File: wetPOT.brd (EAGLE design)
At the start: 38.1 x 12.7 mm, 2 parts

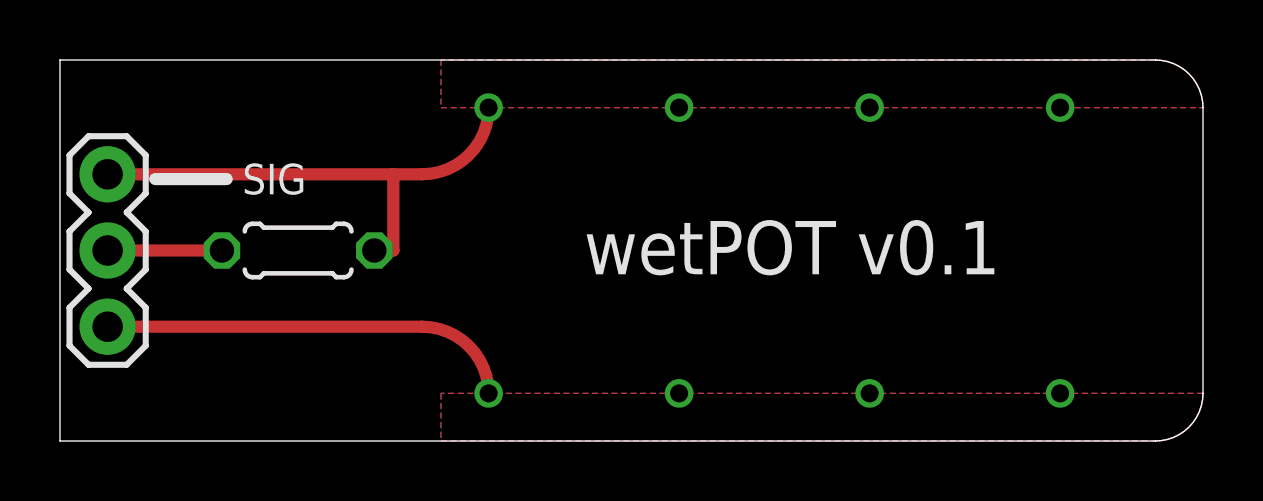
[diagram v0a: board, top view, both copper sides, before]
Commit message: Updated resistor to correct form factor.
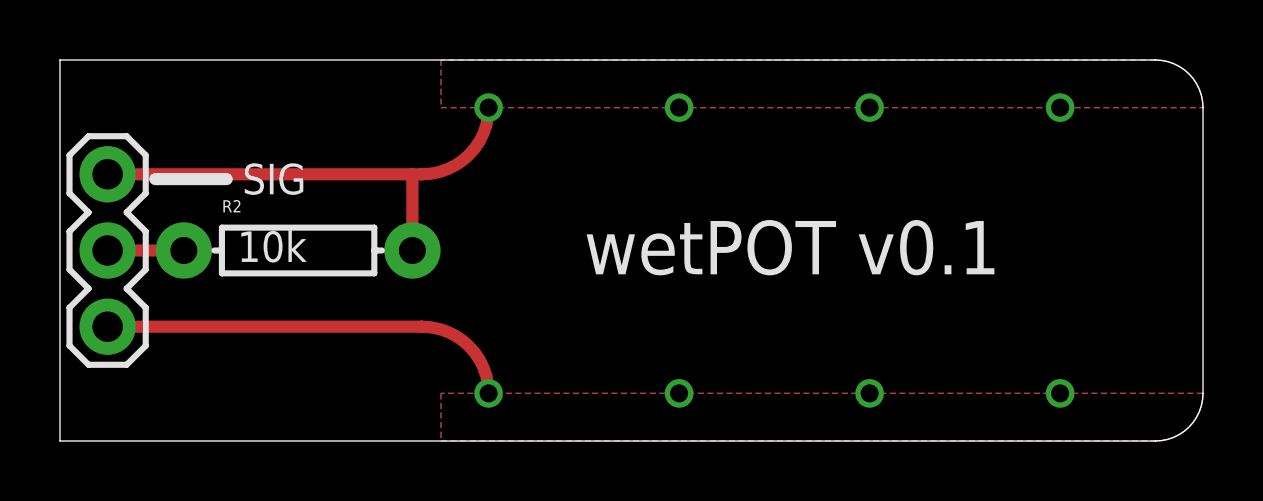
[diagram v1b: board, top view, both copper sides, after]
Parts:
- removed R1: 10k, resistor:0204/5
- added R2: 10k, SparkFun-Resistors:AXIAL-0.3
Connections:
- net PIN0: now also R2.P$2; no longer R1.2
- net PIN1: now also R2.P$1; no longer R1.1
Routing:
- net PIN1: track 3.81 -> 2.54 mm
- net PIN0: track 16.8 -> 16.2 mm
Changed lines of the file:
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@@
 <grid distance="0.03125" unitdist="inch" unit="inch" style="lines" multiple="1" display="yes" altdistance="0.025" altunitdist="inch" altunit="inch"/>
 <layers>
-<layer number="1" name="Top" color="4" fill="1" visible="no" active="yes"/>
-<layer number="16" name="Bottom" color="1" fill="1" visible="no" active="yes"/>
+<layer number="1" name="Top" color="4" fill="1" visible="yes" active="yes"/>
+<layer number="16" name="Bottom" color="1" fill="1" visible="yes" active="yes"/>
 <layer number="17" name="Pads" color="2" fill="1" visible="yes" active="yes"/>
 <layer number="18" name="Vias" color="2" fill="1" visible="yes" active="yes"/>
@@
 <layer number="223" name="223bmp" color="24" fill="1" visible="no" active="no"/>
 <layer number="224" name="224bmp" color="25" fill="1" visible="no" active="no"/>
+<layer number="225" name="225bmp" color="7" fill="1" visible="yes" active="yes"/>
+<layer number="226" name="226bmp" color="7" fill="1" visible="yes" active="yes"/>
+<layer number="227" name="227bmp" color="7" fill="1" visible="yes" active="yes"/>
+<layer number="228" name="228bmp" color="7" fill="1" visible="yes" active="yes"/>
+<layer number="229" name="229bmp" color="7" fill="1" visible="yes" active="yes"/>
+<layer number="230" name="230bmp" color="7" fill="1" visible="yes" active="yes"/>
+<layer number="231" name="231bmp" color="7" fill="1" visible="yes" active="yes"/>
 <layer number="248" name="Housing" color="7" fill="1" visible="yes" active="yes"/>
 <layer number="249" name="Edge" color="7" fill="1" visible="yes" active="yes"/>
@@
 </autorouter>
 <elements>
-<element name="R1" library="resistor" package="0204/5" value="10k" x="7.9375" y="6.35" smashed="yes"/>
 <element name="JP2" library="SparkFun-Connectors" package="1X03" value="" x="1.5875" y="3.81" smashed="yes" rot="R90">
 <attribute name="VALUE" x="4.7625" y="2.54" size="1.27" layer="27" rot="R90"/>
+</element>
+<element name="R2" library="SparkFun-Resistors" package="AXIAL-0.3" value="10k" x="7.9375" y="6.35">
+<attribute name="PROD_ID" value="RES-12183" x="7.9375" y="6.35" size="1.778" layer="27" display="off"/>
 </element>
 </elements>
 <signals>
 <signal name="PIN0">
-<contactref element="R1" pad="2"/>
 <contactref element="JP2" pad="3"/>
 <polygon width="0.4064" layer="1">
@@
 <via x="26.9875" y="11.1125" extent="1-16" drill="0.6" shape="octagon"/>
 <via x="33.3375" y="11.1125" extent="1-16" drill="0.6" shape="octagon"/>
-<wire x1="1.5875" y1="8.89" x2="11.1125" y2="8.89" width="0.4064" layer="1"/>
-<wire x1="11.1125" y1="8.89" x2="12.065" y2="8.89" width="0.4064" layer="1"/>
+<wire x1="1.5875" y1="8.89" x2="11.7475" y2="8.89" width="0.4064" layer="1"/>
 <wire x1="12.065" y1="8.89" x2="14.2875" y2="11.1125" width="0.4064" layer="1" curve="90"/>
-<wire x1="10.4775" y1="6.35" x2="11.1125" y2="6.35" width="0.4064" layer="1"/>
-<wire x1="11.1125" y1="6.35" x2="11.1125" y2="8.89" width="0.4064" layer="1"/>
+<contactref element="R2" pad="P$2"/>
+<wire x1="12.065" y1="8.89" x2="11.7475" y2="8.89" width="0.4064" layer="1"/>
+<wire x1="11.7475" y1="8.89" x2="11.7475" y2="6.35" width="0.4064" layer="1"/>
+<wire x1="26.9875" y1="11.1125" x2="33.3375" y2="11.1125" width="0" layer="19" extent="1-1"/>
+<wire x1="20.6375" y1="11.1125" x2="26.9875" y2="11.1125" width="0" layer="19" extent="1-1"/>
+<wire x1="14.2875" y1="11.1125" x2="20.6375" y2="11.1125" width="0" layer="19" extent="1-1"/>
 </signal>
 <signal name="PIN1">
-<contactref element="R1" pad="1"/>
 <contactref element="JP2" pad="2"/>
-<wire x1="1.5875" y1="6.35" x2="5.3975" y2="6.35" width="0.4064" layer="1"/>
+<contactref element="R2" pad="P$1"/>
+<wire x1="4.1275" y1="6.35" x2="1.5875" y2="6.35" width="0.4064" layer="1"/>
 </signal>
 <signal name="N$4">

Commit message: Turned resistor 90° to try and keep it out of the dirt.
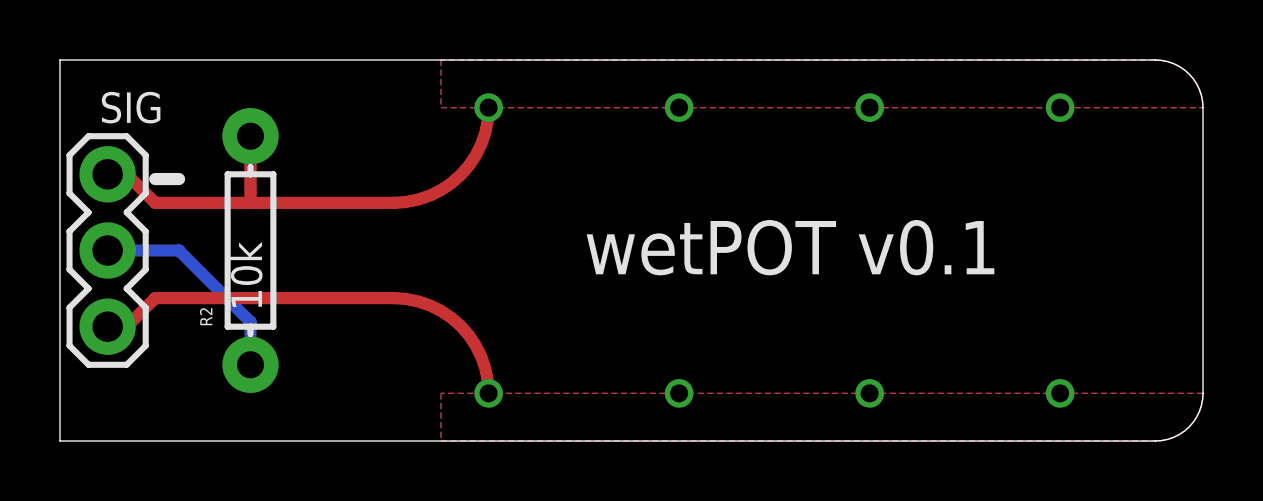
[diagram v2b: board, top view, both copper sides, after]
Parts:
- moved R2 1.59 mm to (6.35, 6.35), turned to 90 degrees
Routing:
- net PIN1: track 2.54 -> 7.18 mm
- net PIN2: track 13.6 -> 14.4 mm
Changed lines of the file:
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@@
 <wire x1="36.5125" y1="12.7" x2="0" y2="12.7" width="0" layer="20"/>
 <wire x1="0" y1="12.7" x2="0" y2="0" width="0" layer="20"/>
-<text x="7.14375" y="8.73125" size="1.016" layer="121" rot="R180" align="center">SIG</text>
-<wire x1="3.175" y1="8.73125" x2="5.55625" y2="8.73125" width="0.4064" layer="121"/>
+<text x="2.38125" y="11.1125" size="1.016" layer="121" rot="R180" align="center">SIG</text>
+<wire x1="3.175" y1="8.73125" x2="3.96875" y2="8.73125" width="0.4064" layer="121"/>
 <text x="17.4625" y="5.55625" size="1.778" layer="121">wetPOT v0.1</text>
 <polygon width="0.4064" layer="29">
@@
 <attribute name="VALUE" x="4.7625" y="2.54" size="1.27" layer="27" rot="R90"/>
 </element>
-<element name="R2" library="SparkFun-Resistors" package="AXIAL-0.3" value="10k" x="7.9375" y="6.35">
-<attribute name="PROD_ID" value="RES-12183" x="7.9375" y="6.35" size="1.778" layer="27" display="off"/>
+<element name="R2" library="SparkFun-Resistors" package="AXIAL-0.3" value="10k" x="6.35" y="6.35" rot="R90">
+<attribute name="PROD_ID" value="RES-12183" x="6.35" y="6.35" size="1.778" layer="27" rot="R90" display="off"/>
 </element>
 </elements>
@@
 <via x="26.9875" y="11.1125" extent="1-16" drill="0.6" shape="octagon"/>
 <via x="33.3375" y="11.1125" extent="1-16" drill="0.6" shape="octagon"/>
-<wire x1="1.5875" y1="8.89" x2="11.7475" y2="8.89" width="0.4064" layer="1"/>
-<wire x1="12.065" y1="8.89" x2="14.2875" y2="11.1125" width="0.4064" layer="1" curve="90"/>
 <contactref element="R2" pad="P$2"/>
-<wire x1="12.065" y1="8.89" x2="11.7475" y2="8.89" width="0.4064" layer="1"/>
-<wire x1="11.7475" y1="8.89" x2="11.7475" y2="6.35" width="0.4064" layer="1"/>
+<wire x1="3.175" y1="7.9375" x2="6.35" y2="7.9375" width="0.4064" layer="1"/>
+<wire x1="6.35" y1="7.9375" x2="11.1125" y2="7.9375" width="0.4064" layer="1"/>
+<wire x1="11.1125" y1="7.9375" x2="14.2875" y2="11.1125" width="0.4064" layer="1" curve="90"/>
+<wire x1="1.5875" y1="8.89" x2="1.74625" y2="8.73125" width="0.4064" layer="1"/>
+<wire x1="1.74625" y1="8.73125" x2="2.38125" y2="8.73125" width="0.4064" layer="1"/>
+<wire x1="2.38125" y1="8.73125" x2="3.175" y2="7.9375" width="0.4064" layer="1"/>
+<wire x1="6.35" y1="10.16" x2="6.35" y2="7.9375" width="0.4064" layer="1"/>
 <wire x1="26.9875" y1="11.1125" x2="33.3375" y2="11.1125" width="0" layer="19" extent="1-1"/>
 <wire x1="20.6375" y1="11.1125" x2="26.9875" y2="11.1125" width="0" layer="19" extent="1-1"/>
@@
 <contactref element="JP2" pad="2"/>
 <contactref element="R2" pad="P$1"/>
-<wire x1="4.1275" y1="6.35" x2="1.5875" y2="6.35" width="0.4064" layer="1"/>
+<wire x1="1.5875" y1="6.35" x2="3.96875" y2="6.35" width="0.4064" layer="16"/>
+<wire x1="3.96875" y1="6.35" x2="6.35" y2="3.96875" width="0.4064" layer="16"/>
+<wire x1="6.35" y1="3.96875" x2="6.35" y2="2.54" width="0.4064" layer="16"/>
 </signal>
 <signal name="N$4">
@@
 <vertex x="38.1" y="1.5875"/>
 </polygon>
-<wire x1="1.5875" y1="3.81" x2="12.065" y2="3.81" width="0.4064" layer="1"/>
-<wire x1="12.065" y1="3.81" x2="14.2875" y2="1.5875" width="0.4064" layer="1" curve="-90"/>
+<wire x1="3.175" y1="4.7625" x2="11.1125" y2="4.7625" width="0.4064" layer="1"/>
+<wire x1="11.1125" y1="4.7625" x2="14.2875" y2="1.5875" width="0.4064" layer="1" curve="-90"/>
+<wire x1="1.5875" y1="3.81" x2="1.74625" y2="3.96875" width="0.4064" layer="1"/>
+<wire x1="1.74625" y1="3.96875" x2="2.38125" y2="3.96875" width="0.4064" layer="1"/>
+<wire x1="2.38125" y1="3.96875" x2="3.175" y2="4.7625" width="0.4064" layer="1"/>
+<wire x1="26.9875" y1="1.5875" x2="33.3375" y2="1.5875" width="0" layer="19" extent="1-1"/>
+<wire x1="20.6375" y1="1.5875" x2="26.9875" y2="1.5875" width="0" layer="19" extent="1-1"/>
+<wire x1="14.2875" y1="1.5875" x2="20.6375" y2="1.5875" width="0" layer="19" extent="1-1"/>
 </signal>
 </signals>

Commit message: Updated rev number on silkscreen and board layout.
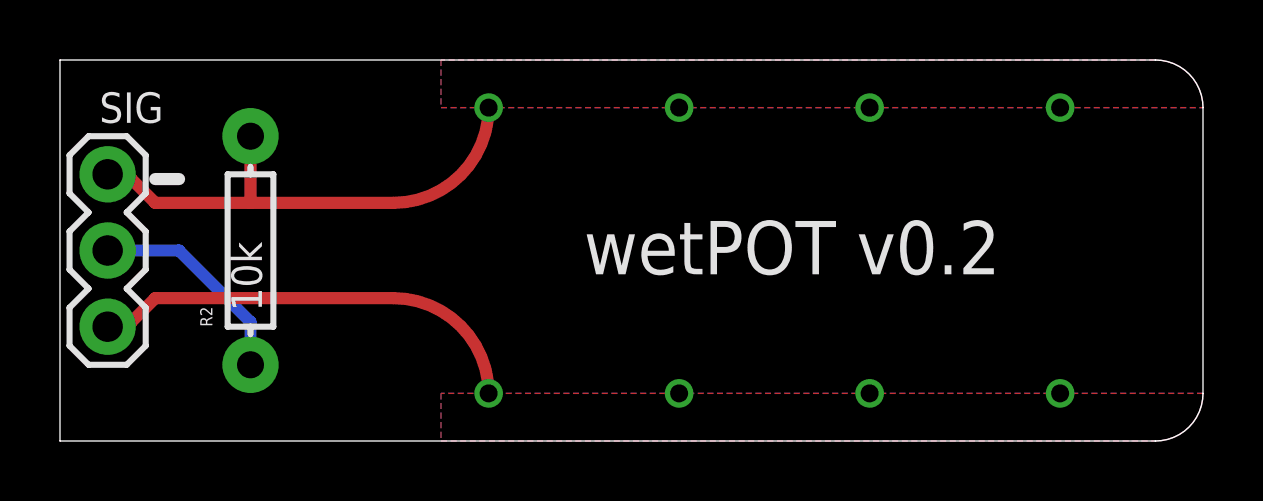
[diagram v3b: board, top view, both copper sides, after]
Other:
- board text added: "wetPOT v0.2"
- board text removed: "wetPOT v0.1"
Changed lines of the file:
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@@
 <text x="2.38125" y="11.1125" size="1.016" layer="121" rot="R180" align="center">SIG</text>
 <wire x1="3.175" y1="8.73125" x2="3.96875" y2="8.73125" width="0.4064" layer="121"/>
-<text x="17.4625" y="5.55625" size="1.778" layer="121">wetPOT v0.1</text>
+<text x="17.4625" y="5.55625" size="1.778" layer="121">wetPOT v0.2</text>
 <polygon width="0.4064" layer="29">
 <vertex x="12.7" y="1.5875"/>
